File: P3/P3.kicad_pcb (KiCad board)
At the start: 2 copper layers, 86.4 x 45.7 mm, 32 parts, among them J1 12v, J10 PWR2, J11 r1, J12 r2, J13 inl, J14 inr, J15 outl, J16 outr, J2 Channels, J3 Noritake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

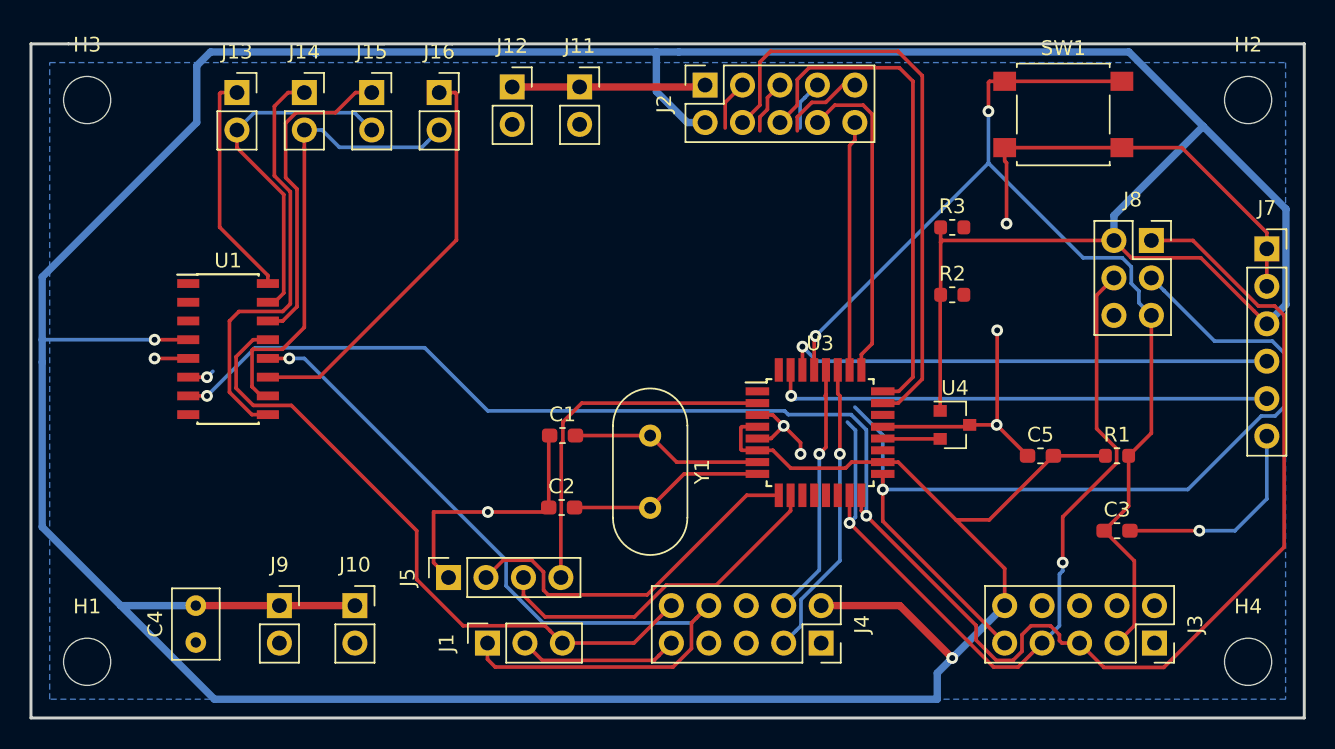
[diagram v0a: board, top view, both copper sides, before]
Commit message: Route P3 PCB
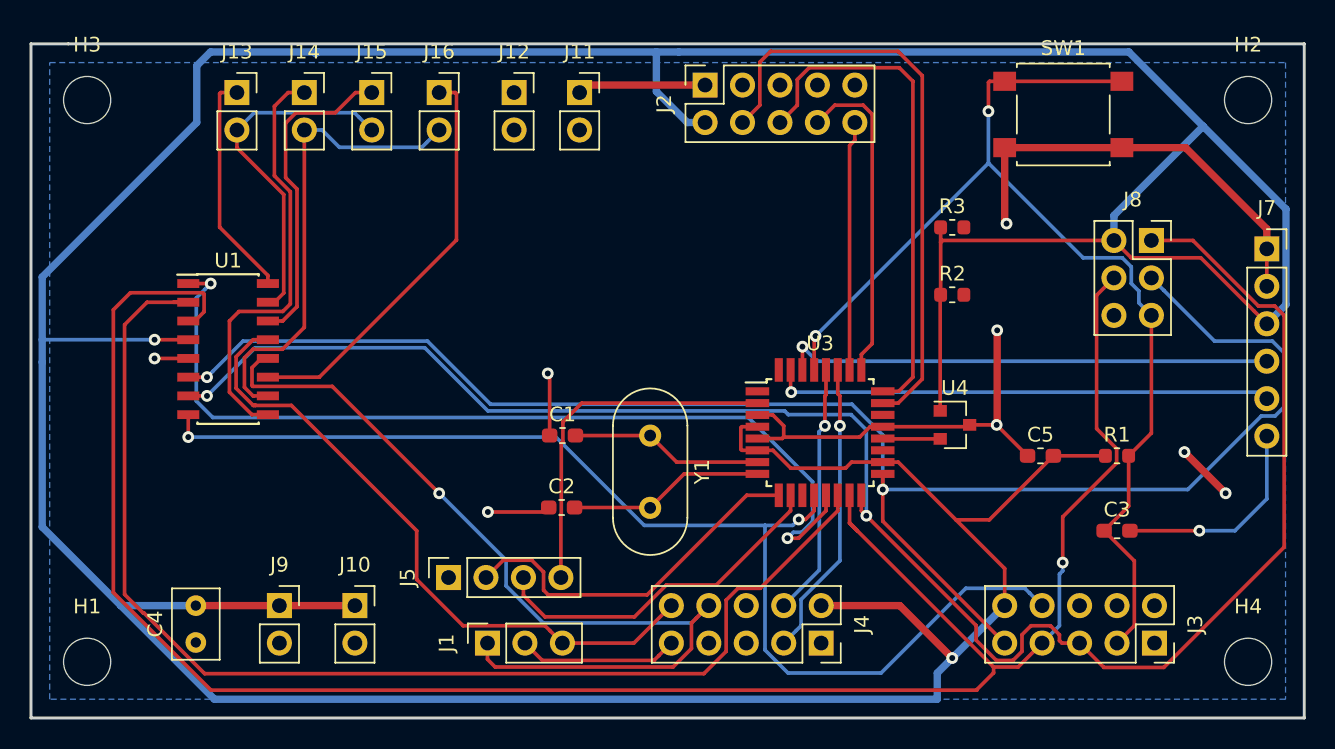
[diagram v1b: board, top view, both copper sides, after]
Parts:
- moved J12 0.40 mm to (103.9, 61.7)
- moved J11 0.38 mm to (108.3, 61.7)
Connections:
- J1 pad 1: (no net) -> /+12v
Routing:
- net /MOSI: track 54.8 -> 140.8 mm, vias 2 -> 1
- net /SS: track 0.00 -> 82.5 mm
- net /PB0: track 0.00 -> 78.7 mm, vias 0 -> 2
- net /PB1: track 0.00 -> 63.3 mm, vias 0 -> 2
- net /SCK: track 67.4 -> 113.7 mm
- net (no net): track 16.2 -> 0.00 mm
- net GND: track 85.9 -> 81.5 mm, vias 7 -> 8
- net /+12v: track 57.9 -> 60.8 mm
- net /AGNDR: track 31.5 -> 32.7 mm

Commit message: Add capsensor, humidity sensor p3, garduino with avr
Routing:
- net GND: track 81.5 -> 86.4 mm
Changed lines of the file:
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@@
     (thickness 1.6)
     (drawings 5)
-    (tracks 441)
+    (tracks 443)
     (zones 0)
     (modules 32)
@@
   (segment (start 122.07788 85.18612) (end 122.174 85.09) (width 0.25) (layer F.Cu) (net 3))
   (segment (start 120.39092 85.18612) (end 122.07788 85.18612) (width 0.25) (layer F.Cu) (net 3))
+  (segment (start 106.29776 89.80424) (end 106.2368 89.8652) (width 0.25) (layer F.Cu) (net 3))
+  (segment (start 106.29776 84.98332) (end 106.29776 89.80424) (width 0.25) (layer F.Cu) (net 3))
   (segment (start 145.955001 93.490001) (end 143.905 91.44) (width 0.25) (layer F.Cu) (net 4) (status 20))
   (segment (start 145.955001 97.884999) (end 145.955001 93.490001) (width 0.25) (layer F.Cu) (net 4))

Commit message: Add water-switches
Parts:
- removed J11: r1, Connector_PinSocket_2.54mm:PinSocket_1x02_P2.54mm_Vertical
- removed J12: r2, Connector_PinSocket_2.54mm:PinSocket_1x02_P2.54mm_Vertical
- C1, C2, R2, R3: moved to B.Cu
- moved C1 8.24 mm to (113.9, 80.3), turned to 180 degrees
- moved C2 6.82 mm to (112.1, 94.5)
- moved R3 3.09 mm to (134.1, 73.9), turned to 180 degrees
- moved R2 2.84 mm to (134.1, 78.2), turned to 180 degrees
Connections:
- J2 pad 3: (no net) -> /PD2
- J2 pad 5: (no net) -> /PD3
- J2 pad 7: (no net) -> /PB0
- J2 pad 9: (no net) -> /PB1
- J4 pad 5: (no net) -> /PD7
- R2 pad 2: (no net) -> /SDA
- R3 pad 2: (no net) -> /SCL
- U1 pad 1: /PB1 -> +5V
- U3 pad 1: (no net) -> /PD3
- U3 pad 11: (no net) -> /PD7
- U3 pad 32: (no net) -> /PD2
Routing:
- net /PB1: track 63.3 -> 2.48 mm, vias 2 -> 1
- net /PB0: track 78.7 -> 106.6 mm, vias 2 -> 5
- net /PD3: track 0.00 -> 21.4 mm
- net /PD2: track 0.00 -> 20.3 mm, vias 0 -> 1
- net /PD7: track 0.00 -> 13.1 mm, vias 0 -> 1
- net /SCL: track 17.2 -> 29.3 mm, vias 1 -> 2
- net GND: track 86.4 -> 76.7 mm, vias 8 -> 13
- net /SDA: track 20.2 -> 29.8 mm, vias 1 -> 2
- net /MISO: track 123.2 -> 117.2 mm
- net +5V: track 326.1 -> 332.0 mm, vias 2 -> 3
- net /SS: track 82.5 -> 86.1 mm
- net /ADC0: track 40.5 -> 39.4 mm
- net /SCK: track 113.7 -> 114.7 mm
- net (no net): track 0.00 -> 0.89 mm
